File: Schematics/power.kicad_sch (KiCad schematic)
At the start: 6 parts, among them U3 PowerIn, U4 LDL1117-3.3

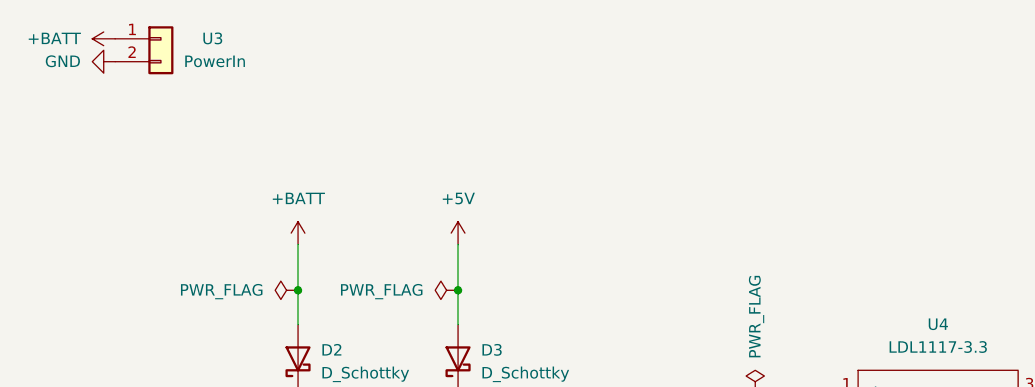
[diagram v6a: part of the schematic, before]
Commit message: began routing, need layout approval
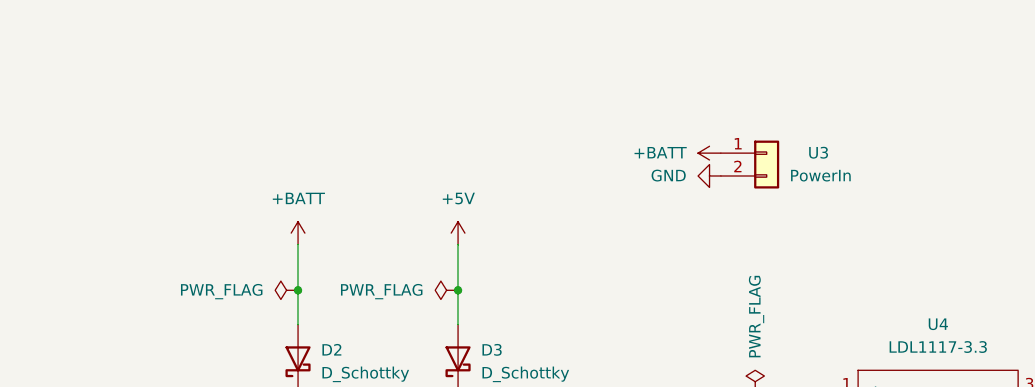
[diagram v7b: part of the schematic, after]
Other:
- moved on the sheet: U3
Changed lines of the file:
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@@
 	(symbol
 		(lib_id "Connector_Generic:Conn_01x02")
-		(at 63.5 40.64 0)
+		(at 130.81 53.34 0)
 		(unit 1)
 		(exclude_from_sim no)
@@
 		(dnp no)
 		(property "Reference" "U3"
-			(at 68.072 40.64 0)
+			(at 135.382 53.34 0)
 			(effects
 				(font
@@
 		)
 		(property "Value" "PowerIn"
-			(at 66.04 43.1799 0)
+			(at 133.35 55.8799 0)
 			(effects
 				(font
@@
 		)
 		(property "Footprint" "myFootprints:MOLEX_26013114"
-			(at 63.5 40.64 0)
+			(at 130.81 53.34 0)
 			(effects
 				(font
@@
 		)
 		(property "Datasheet" "~"
-			(at 63.5 40.64 0)
+			(at 130.81 53.34 0)
 			(effects
 				(font
@@
 		)
 		(property "Description" "Generic connector, single row, 01x02, script generated (kicad-library-utils/schlib/autogen/connector/)"
-			(at 63.5 40.64 0)
+			(at 130.81 53.34 0)
 			(effects
 				(font
@@
 		)
 		(property "LCSC Part" "C17644051"
-			(at 63.5 40.64 0)
+			(at 130.81 53.34 0)
 			(effects
 				(font
@@
 		)
 		(property "Description_1" ""
-			(at 63.5 40.64 0)
+			(at 130.81 53.34 0)
 			(effects
 				(font
@@
 		)
 		(property "MF" ""
-			(at 63.5 40.64 0)
+			(at 130.81 53.34 0)
 			(effects
 				(font
@@
 		)
 		(property "MP" ""
-			(at 63.5 40.64 0)
+			(at 130.81 53.34 0)
 			(effects
 				(font
@@
 		)
 		(property "Package" ""
-			(at 63.5 40.64 0)
+			(at 130.81 53.34 0)
 			(effects
 				(font
@@
 		)
 		(property "Price" ""
-			(at 63.5 40.64 0)
+			(at 130.81 53.34 0)
 			(effects
 				(font
@@
 		)
 		(property "Purchase-URL" ""
-			(at 63.5 40.64 0)
+			(at 130.81 53.34 0)
 			(effects
 				(font
@@
 	(symbol
 		(lib_id "power:+BATT")
-		(at 58.42 40.64 90)
+		(at 125.73 53.34 90)
 		(unit 1)
 		(exclude_from_sim no)
@@
 		(fields_autoplaced yes)
 		(property "Reference" "#PWR040"
-			(at 62.23 40.64 0)
+			(at 129.54 53.34 0)
 			(effects
 				(font
@@
 		)
 		(property "Value" "+BATT"
-			(at 54.61 40.6399 90)
+			(at 121.92 53.3399 90)
 			(effects
 				(font
@@
 		)
 		(property "Footprint" ""
-			(at 58.42 40.64 0)
+			(at 125.73 53.34 0)
 			(effects
 				(font
@@
 		)
 		(property "Datasheet" ""
-			(at 58.42 40.64 0)
+			(at 125.73 53.34 0)
 			(effects
 				(font
@@
 		)
 		(property "Description" "Power symbol creates a global label with name \"+BATT\""
-			(at 58.42 40.64 0)
+			(at 125.73 53.34 0)
 			(effects
 				(font
@@
 	(symbol
 		(lib_id "power:GND")
-		(at 58.42 43.18 270)
+		(at 125.73 55.88 270)
 		(unit 1)
 		(exclude_from_sim no)
@@
 		(fields_autoplaced yes)
 		(property "Reference" "#PWR041"
-			(at 52.07 43.18 0)
+			(at 119.38 55.88 0)
 			(effects
 				(font
@@
 		)
 		(property "Value" "GND"
-			(at 54.61 43.1799 90)
+			(at 121.92 55.8799 90)
 			(effects
 				(font
@@
 		)
 		(property "Footprint" ""
-			(at 58.42 43.18 0)
+			(at 125.73 55.88 0)
 			(effects
 				(font
@@
 		)
 		(property "Datasheet" ""
-			(at 58.42 43.18 0)
+			(at 125.73 55.88 0)
 			(effects
 				(font
@@
 		)
 		(property "Description" "Power symbol creates a global label with name \"GND\" , ground"
-			(at 58.42 43.18 0)
-			(effects
-				(font
+			(at 125.73 55.88 0)
+			(effects
+				(font

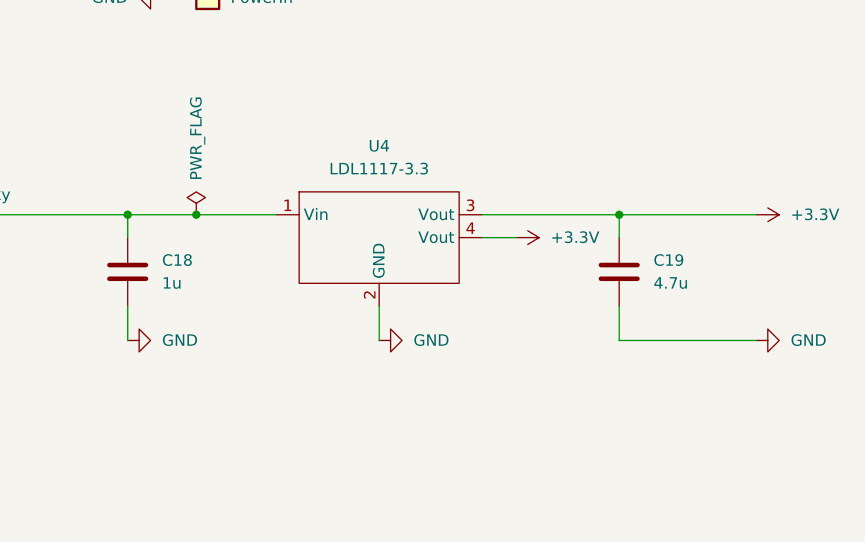
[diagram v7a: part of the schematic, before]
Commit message: fixing DRC Warnings updated USBC footprint/schematic, did impedance matching for the trace from rfm95 to antenna connector fixed resistor on flash memeory
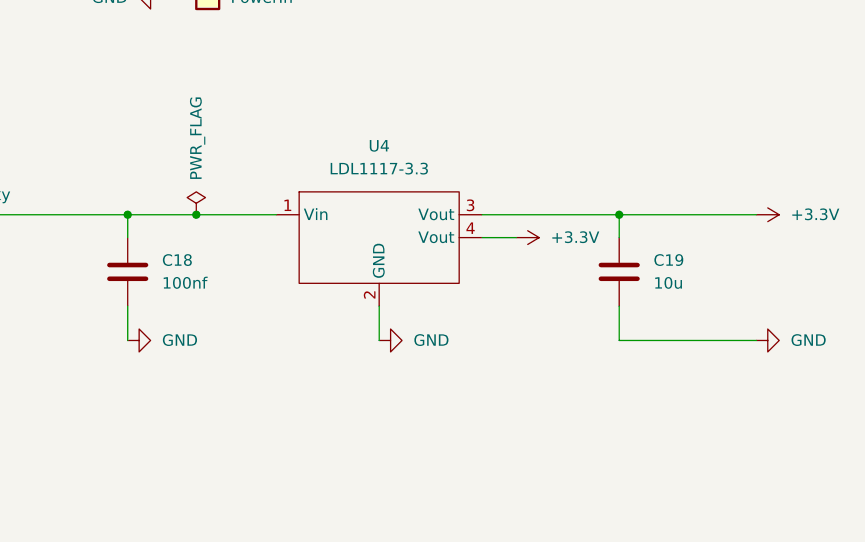
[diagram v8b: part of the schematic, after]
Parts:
- C18: value 1u -> 100nf
- C19: value 4.7u -> 10u
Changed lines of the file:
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@@
 			)
 		)
-		(property "Value" "4.7u"
+		(property "Value" "10u"
 			(at 180.34 87.6299 0)
 			(effects
@@
 			)
 		)
-		(property "Value" "1u"
+		(property "Value" "100nf"
 			(at 125.73 87.6299 0)
 			(effects
